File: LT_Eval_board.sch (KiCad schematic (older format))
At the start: 0 parts

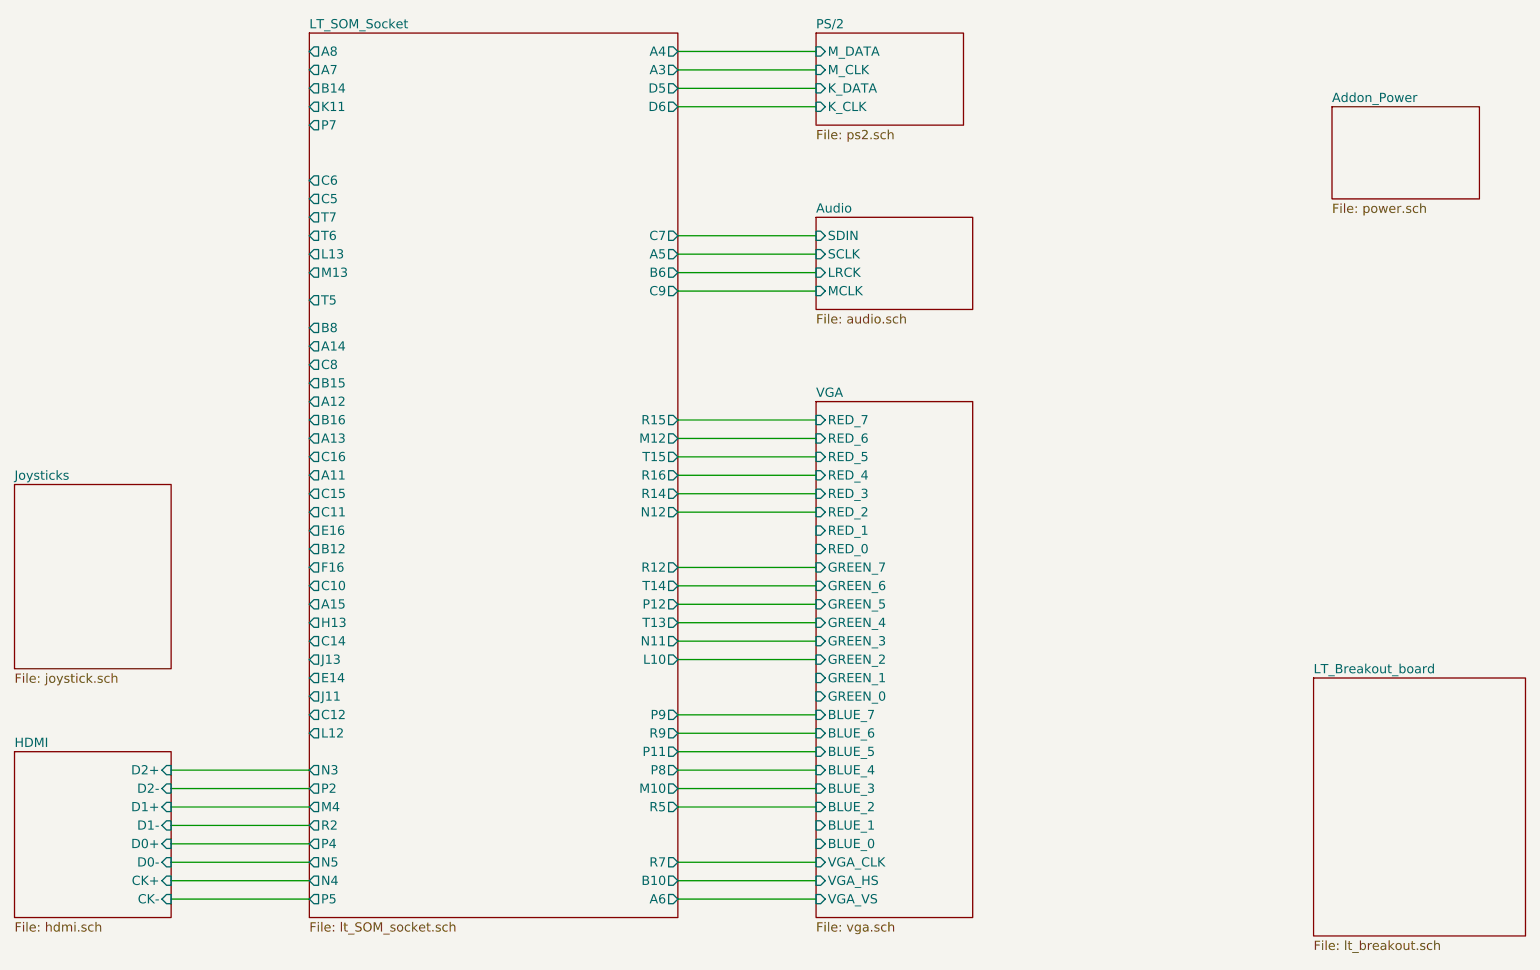
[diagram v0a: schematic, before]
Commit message: Joystick net assigned.
Signed-off-by: Kali Prasad <kprasadvnsi@protonmail.com>
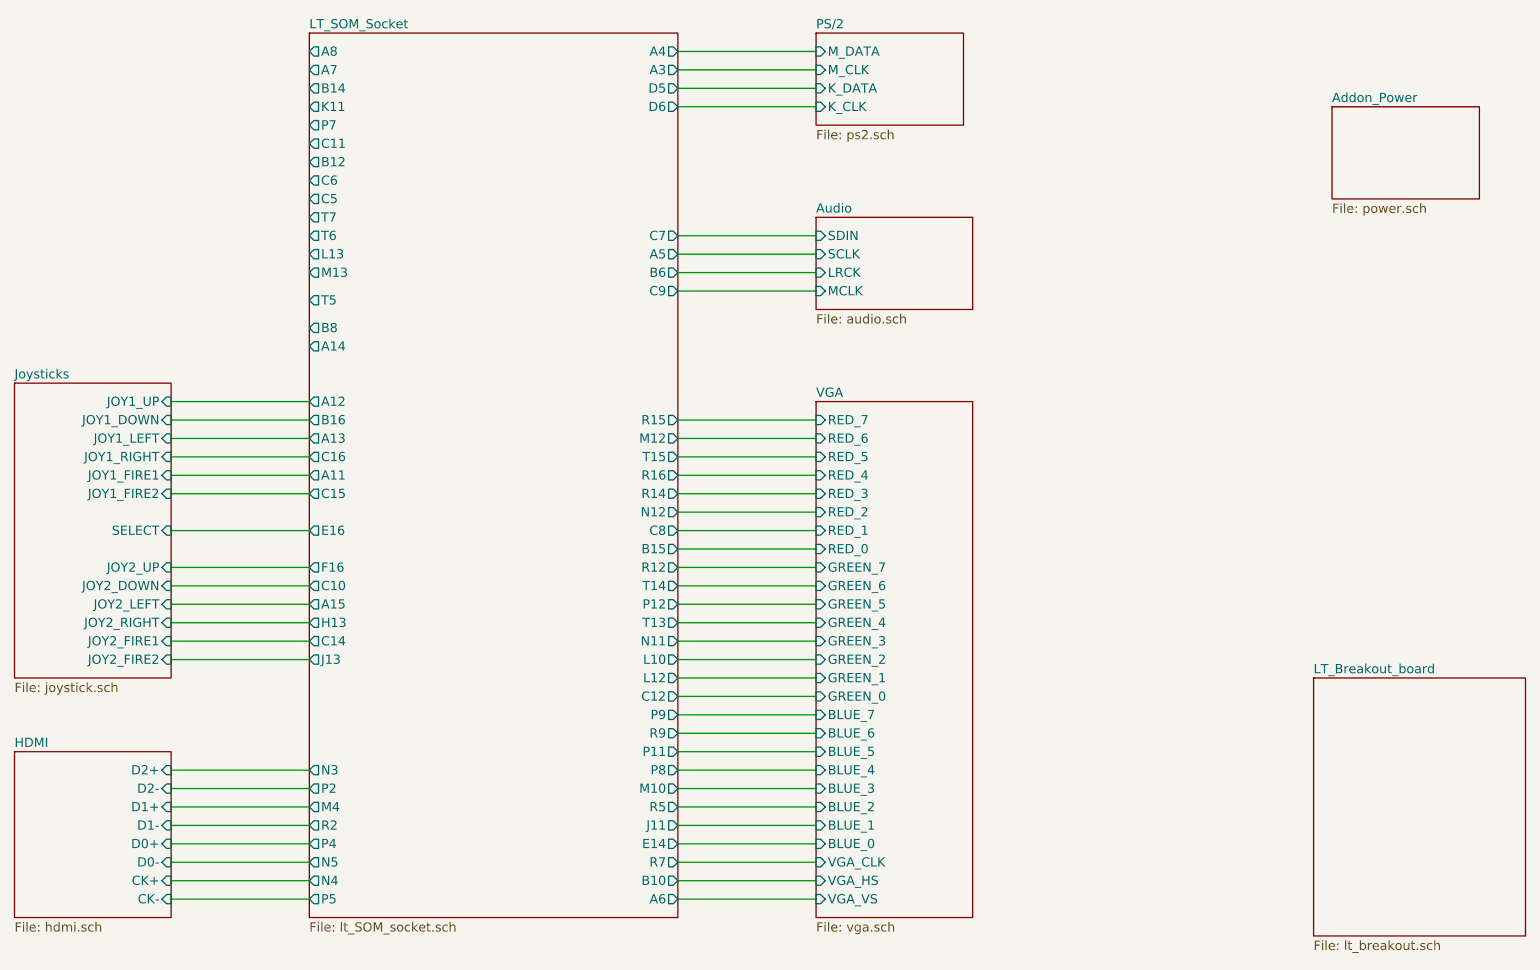
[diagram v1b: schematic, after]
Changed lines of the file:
@@
 F17 "B8" O L 3700 2700 50
 F18 "A14" O L 3700 2800 50
-F19 "C8" O L 3700 2900 50
-F20 "B15" O L 3700 3000 50
+F19 "C8" O R 5700 3800 50
+F20 "B15" O R 5700 3900 50
 F21 "A12" O L 3700 3100 50
 F22 "B16" O L 3700 3200 50
@@
 F25 "A11" O L 3700 3500 50
 F26 "C15" O L 3700 3600 50
-F27 "C11" O L 3700 3700 50
+F27 "C11" O L 3700 1700 50
 F28 "E16" O L 3700 3800 50
-F29 "B12" O L 3700 3900 50
+F29 "B12" O L 3700 1800 50
 F30 "F16" O L 3700 4000 50
 F31 "C10" O L 3700 4100 50
@@
 F34 "C14" O L 3700 4400 50
 F35 "J13" O L 3700 4500 50
-F36 "E14" O L 3700 4600 50
-F37 "J11" O L 3700 4700 50
-F38 "C12" O L 3700 4800 50
-F39 "L12" O L 3700 4900 50
+F36 "E14" O R 5700 5500 50
+F37 "J11" O R 5700 5400 50
+F38 "C12" O R 5700 4700 50
+F39 "L12" O R 5700 4600 50
 F40 "N3" O L 3700 5100 50
 F41 "P2" O L 3700 5200 50
@@
 $EndSheet
 $Sheet
-S 2100 3550 850  1000
+S 2100 3000 850  1600
 U 5D187063
 F0 "Joysticks" 50
 F1 "joystick.sch" 50
-$EndSheet
+F2 "JOY1_UP" I R 2950 3100 50
+F3 "JOY1_DOWN" I R 2950 3200 50
+F4 "JOY1_LEFT" I R 2950 3300 50
+F5 "JOY1_RIGHT" I R 2950 3400 50
+F6 "JOY1_FIRE1" I R 2950 3500 50
+F7 "JOY1_FIRE2" I R 2950 3600 50
+F8 "SELECT" I R 2950 3800 50
+F9 "JOY2_UP" I R 2950 4000 50
+F10 "JOY2_DOWN" I R 2950 4100 50
+F11 "JOY2_LEFT" I R 2950 4200 50
+F12 "JOY2_RIGHT" I R 2950 4300 50
+F13 "JOY2_FIRE1" I R 2950 4400 50
+F14 "JOY2_FIRE2" I R 2950 4500 50
+$EndSheet
+Wire Wire Line
+	2950 4500 3700 4500
+Wire Wire Line
+	2950 4400 3700 4400
+Wire Wire Line
+	2950 4300 3700 4300
+Wire Wire Line
+	2950 4200 3700 4200
+Wire Wire Line
+	2950 4100 3700 4100
+Wire Wire Line
+	2950 4000 3700 4000
+Wire Wire Line
+	2950 3800 3700 3800
+Wire Wire Line
+	2950 3600 3700 3600
+Wire Wire Line
+	2950 3500 3700 3500
+Wire Wire Line
+	2950 3400 3700 3400
+Wire Wire Line
+	2950 3300 3700 3300
+Wire Wire Line
+	2950 3200 3700 3200
+Wire Wire Line
+	2950 3100 3700 3100
+Wire Wire Line
+	5700 3800 6450 3800
+Wire Wire Line
+	5700 3900 6450 3900
+Wire Wire Line
+	5700 4600 6450 4600
+Wire Wire Line
+	5700 4700 6450 4700
+Wire Wire Line
+	5700 5400 6450 5400
+Wire Wire Line
+	5700 5500 6450 5500
 $EndSCHEMATC
